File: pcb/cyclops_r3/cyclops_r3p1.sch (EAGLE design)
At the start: 48 parts, among them Q1 SUM11006, Q2 IRF510, U1 MCP4921, U2 317-N, U3 ADR03, U4 OP1177, U5 LM324N, U6 ZXTD45

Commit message: Minor changes.
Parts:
- removed R14: 560, cyclops:R_0603
- added R12: 560, cyclops:R_0603
- R10: value 1.1k -> 560
- R11: value 560 -> 1.1k
- renumbered C16 to C15
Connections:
- net +12V: now also R11.2; no longer R10.2
- net GND: now also R12.1; no longer R11.1
- net N$10: now also R10.1; no longer R14.1
- net N$13: now also R10.2, R11.1, R12.2; no longer R10.1, R11.2, R14.2
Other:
- note added: "GND LINK"
- moved on the sheet: R10, R11
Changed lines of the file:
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@@
 <part name="R5" library="cyclops" deviceset="R" device="_0603" value="470"/>
 <part name="R6" library="cyclops" deviceset="R" device="_0603" value="1k"/>
-<part name="C16" library="cyclops" deviceset="C" device="_0805" value="1uF"/>
+<part name="C15" library="cyclops" deviceset="C" device="_0805" value="1uF"/>
 <part name="C14" library="cyclops" deviceset="C" device="_0603" value=".1uF"/>
 <part name="SUPPLY30" library="cyclops" deviceset="AGND" device=""/>
@@
 <part name="SUPPLY31" library="cyclops" deviceset="AGND" device=""/>
 <part name="SUPPLY12" library="cyclops" deviceset="AGND" device=""/>
-<part name="SUPPLY17" library="cyclops" deviceset="AGND" device=""/>
 <part name="SUPPLY34" library="cyclops" deviceset="GND" device=""/>
 <part name="S3" library="cyclops" deviceset="SPDT" device="_CFPA" value="TEST"/>
@@
 <part name="SUPPLY35" library="cyclops" deviceset="AGND" device=""/>
 <part name="Q2" library="cyclops" deviceset="N-MOSFET" device="TO-262" value="IRF510"/>
-<part name="R14" library="cyclops" deviceset="R" device="_0603" value="560"/>
-<part name="R10" library="cyclops" deviceset="R" device="_0603" value="1.1k"/>
-<part name="R11" library="cyclops" deviceset="R" device="_0603" value="560"/>
+<part name="R10" library="cyclops" deviceset="R" device="_0603" value="560"/>
+<part name="R11" library="cyclops" deviceset="R" device="_0603" value="1.1k"/>
+<part name="R12" library="cyclops" deviceset="R" device="_0603" value="560"/>
 <part name="SUPPLY1" library="cyclops" deviceset="AGND" device=""/>
+<part name="SUPPLY4" library="cyclops" deviceset="GND" device=""/>
+<part name="SUPPLY29" library="cyclops" deviceset="GND" device=""/>
 </parts>
 <sheets>
@@
 <description>I/O Interface</description>
 <plain>
+<text x="147.32" y="27.94" size="1.778" layer="97">GND LINK</text>
 </plain>
 <instances>
@@
 <instance part="S1" gate="G$1" x="96.52" y="-33.02" rot="MR0"/>
 <instance part="SUPPLY12" gate="G$1" x="165.1" y="22.86"/>
-<instance part="SUPPLY17" gate="G$1" x="213.36" y="-10.16"/>
-<instance part="SUPPLY34" gate="PE" x="198.12" y="-10.16"/>
+<instance part="SUPPLY34" gate="PE" x="139.7" y="22.86"/>
 <instance part="S3" gate="G$1" x="127" y="-30.48" rot="R180"/>
+<instance part="SUPPLY4" gate="PE" x="60.96" y="10.16"/>
+<instance part="SUPPLY29" gate="PE" x="38.1" y="83.82"/>
 </instances>
 <busses>
@@
 <pinref part="U$1" gate="G$1" pin="5V"/>
 <wire x1="58.42" y1="17.78" x2="58.42" y2="12.7" width="0.1524" layer="91"/>
+<wire x1="58.42" y1="12.7" x2="53.34" y2="12.7" width="0.1524" layer="91"/>
+<label x="53.34" y="12.7" size="1.778" layer="95"/>
 </segment>
 </net>
@@
 <pinref part="U$1" gate="G$1" pin="D4"/>
 <wire x1="71.12" y1="78.74" x2="71.12" y2="91.44" width="0.1524" layer="91"/>
-<label x="71.12" y="83.82" size="1.778" layer="95" rot="R90"/>
+<label x="78.74" y="91.44" size="1.778" layer="95"/>
+<wire x1="71.12" y1="91.44" x2="86.36" y2="91.44" width="0.1524" layer="91"/>
 </segment>
 </net>
@@
 <segment>
 <pinref part="SUPPLY34" gate="PE" pin="GND"/>
-<wire x1="198.12" y1="-7.62" x2="198.12" y2="-2.54" width="0.1524" layer="91"/>
-<pinref part="SUPPLY17" gate="G$1" pin="AGND"/>
-<wire x1="198.12" y1="-2.54" x2="213.36" y2="-2.54" width="0.1524" layer="91"/>
-<wire x1="213.36" y1="-2.54" x2="213.36" y2="-7.62" width="0.1524" layer="91"/>
+<wire x1="139.7" y1="25.4" x2="139.7" y2="30.48" width="0.1524" layer="91"/>
+<wire x1="139.7" y1="30.48" x2="165.1" y2="30.48" width="0.1524" layer="91"/>
+<pinref part="U1" gate="G$1" pin="AVSS"/>
+<wire x1="165.1" y1="25.4" x2="165.1" y2="30.48" width="0.1524" layer="91"/>
+<pinref part="SUPPLY12" gate="G$1" pin="AGND"/>
+<wire x1="165.1" y1="30.48" x2="165.1" y2="33.02" width="0.1524" layer="91"/>
+<junction x="165.1" y="30.48"/>
 </segment>
 <segment>
@@
 </segment>
 <segment>
-<pinref part="U1" gate="G$1" pin="AVSS"/>
-<wire x1="165.1" y1="25.4" x2="165.1" y2="33.02" width="0.1524" layer="91"/>
-<pinref part="SUPPLY12" gate="G$1" pin="AGND"/>
-</segment>
-<segment>
 <pinref part="U$1" gate="G$1" pin="GND$2"/>
 <wire x1="60.96" y1="17.78" x2="60.96" y2="12.7" width="0.1524" layer="91"/>
-</segment>
-<segment>
+<pinref part="SUPPLY4" gate="PE" pin="GND"/>
 <pinref part="U$1" gate="G$1" pin="GND$1"/>
 <wire x1="63.5" y1="17.78" x2="63.5" y2="12.7" width="0.1524" layer="91"/>
-</segment>
-<segment>
+<wire x1="63.5" y1="12.7" x2="60.96" y2="12.7" width="0.1524" layer="91"/>
+<junction x="60.96" y="12.7"/>
+</segment>
+<segment>
+<pinref part="SUPPLY29" gate="PE" pin="GND"/>
+<wire x1="38.1" y1="86.36" x2="38.1" y2="88.9" width="0.1524" layer="91"/>
+<wire x1="38.1" y1="88.9" x2="43.18" y2="88.9" width="0.1524" layer="91"/>
 <pinref part="U$1" gate="G$1" pin="GND"/>
-<wire x1="43.18" y1="78.74" x2="43.18" y2="86.36" width="0.1524" layer="91"/>
+<wire x1="43.18" y1="78.74" x2="43.18" y2="88.9" width="0.1524" layer="91"/>
 </segment>
 </net>
@@
 <instance part="SUPPLY21" gate="G$1" x="40.64" y="93.98"/>
 <instance part="SUPPLY25" gate="G$1" x="53.34" y="93.98"/>
-<instance part="C16" gate="C" x="53.34" y="109.22"/>
+<instance part="C15" gate="C" x="53.34" y="109.22"/>
 <instance part="C14" gate="C" x="40.64" y="109.22"/>
 <instance part="SUPPLY30" gate="G$1" x="-10.16" y="60.96"/>
@@
 <instance part="SUPPLY35" gate="G$1" x="71.12" y="63.5"/>
 <instance part="Q2" gate="G$1" x="165.1" y="86.36"/>
-<instance part="R14" gate="R" x="124.46" y="83.82"/>
-<instance part="R10" gate="R" x="134.62" y="96.52" rot="R90"/>
-<instance part="R11" gate="R" x="134.62" y="71.12" rot="R90"/>
+<instance part="R10" gate="R" x="124.46" y="83.82"/>
+<instance part="R11" gate="R" x="134.62" y="96.52" rot="R90"/>
+<instance part="R12" gate="R" x="134.62" y="71.12" rot="R90"/>
 <instance part="SUPPLY1" gate="G$1" x="134.62" y="45.72"/>
 </instances>
@@
 <segment>
 <pinref part="SUPPLY25" gate="G$1" pin="AGND"/>
-<pinref part="C16" gate="C" pin="2"/>
+<pinref part="C15" gate="C" pin="2"/>
 <wire x1="53.34" y1="96.52" x2="53.34" y2="104.14" width="0.1524" layer="91"/>
 </segment>
@@
 <segment>
 <pinref part="SUPPLY1" gate="G$1" pin="AGND"/>
-<pinref part="R11" gate="R" pin="1"/>
+<pinref part="R12" gate="R" pin="1"/>
 <wire x1="134.62" y1="48.26" x2="134.62" y2="66.04" width="0.1524" layer="91"/>
 </segment>
@@
 <pinref part="C14" gate="C" pin="1"/>
 <wire x1="40.64" y1="121.92" x2="40.64" y2="111.76" width="0.1524" layer="91"/>
-<pinref part="C16" gate="C" pin="1"/>
+<pinref part="C15" gate="C" pin="1"/>
 <wire x1="40.64" y1="121.92" x2="53.34" y2="121.92" width="0.1524" layer="91"/>
 <wire x1="53.34" y1="121.92" x2="53.34" y2="111.76" width="0.1524" layer="91"/>
@@
 <junction x="66.04" y="121.92"/>
 <label x="147.32" y="121.92" size="1.778" layer="95"/>
-<pinref part="R10" gate="R" pin="2"/>
+<pinref part="R11" gate="R" pin="2"/>
 <wire x1="134.62" y1="121.92" x2="167.64" y2="121.92" width="0.1524" layer="91"/>
 <wire x1="134.62" y1="101.6" x2="134.62" y2="121.92" width="0.1524" layer="91"/>
@@
 <wire x1="114.3" y1="83.82" x2="114.3" y2="76.2" width="0.1524" layer="91"/>
 <wire x1="114.3" y1="76.2" x2="109.22" y2="76.2" width="0.1524" layer="91"/>
-<pinref part="R14" gate="R" pin="1"/>
+<pinref part="R10" gate="R" pin="1"/>
 <wire x1="119.38" y1="83.82" x2="114.3" y2="83.82" width="0.1524" layer="91"/>
 <junction x="114.3" y="83.82"/>
@@
 <segment>
 <pinref part="Q2" gate="G$1" pin="G"/>
-<pinref part="R14" gate="R" pin="2"/>
+<pinref part="R10" gate="R" pin="2"/>
 <wire x1="162.56" y1="83.82" x2="134.62" y2="83.82" width="0.1524" layer="91"/>
-<pinref part="R10" gate="R" pin="1"/>
+<pinref part="R11" gate="R" pin="1"/>
 <wire x1="134.62" y1="83.82" x2="129.54" y2="83.82" width="0.1524" layer="91"/>
 <wire x1="134.62" y1="83.82" x2="134.62" y2="91.44" width="0.1524" layer="91"/>
 <junction x="134.62" y="83.82"/>
-<pinref part="R11" gate="R" pin="2"/>
+<pinref part="R12" gate="R" pin="2"/>
 <wire x1="134.62" y1="83.82" x2="134.62" y2="76.2" width="0.1524" layer="91"/>
 </segment>
@@
 </sheet>
 </sheets>
+<errors>
+</errors>
 </schematic>
 </drawing>

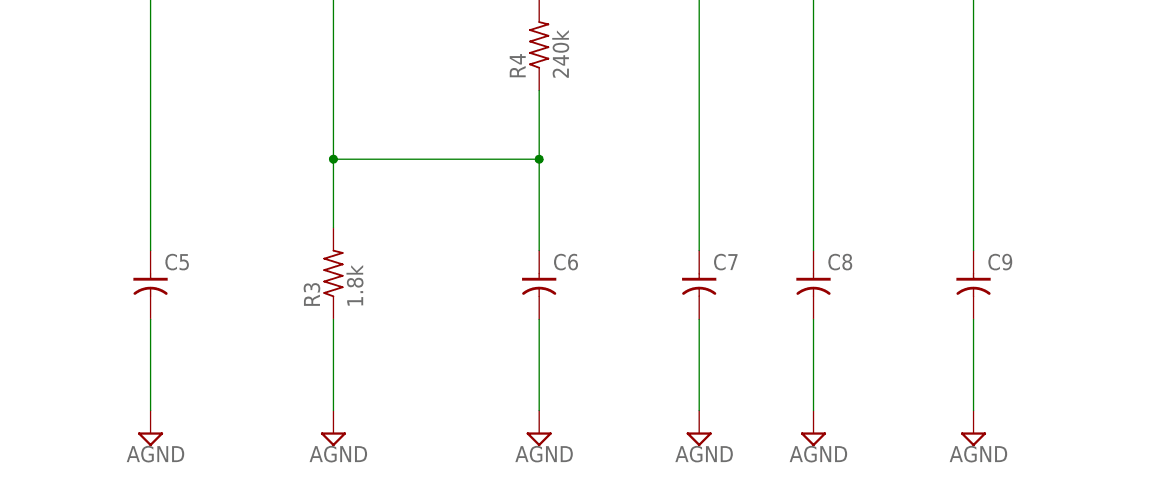
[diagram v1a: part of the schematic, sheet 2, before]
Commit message: Small routing improvement.
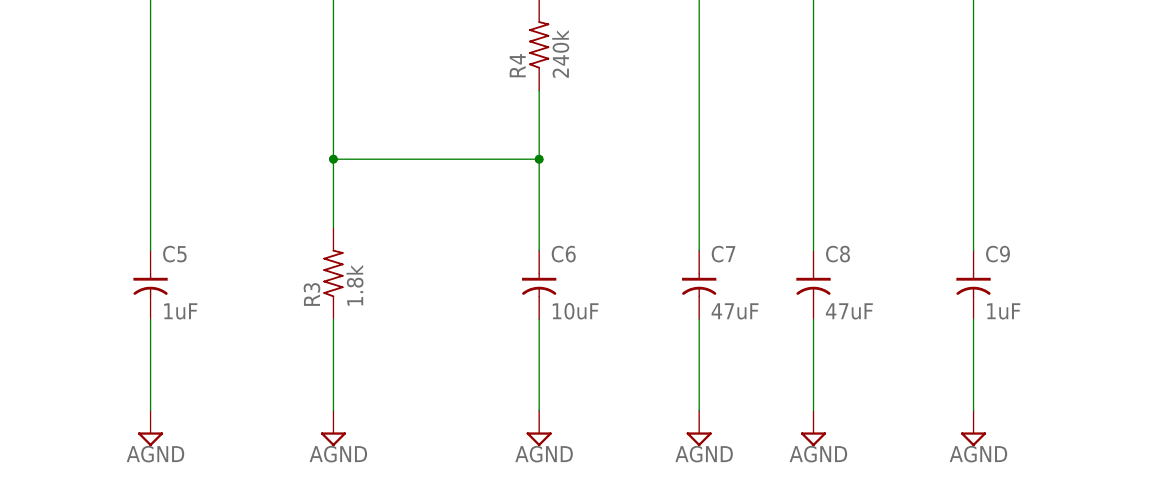
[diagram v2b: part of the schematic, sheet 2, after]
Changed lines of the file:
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@@
 <instance part="SUPPLY9" gate="G$1" x="86.36" y="-58.42"/>
 <instance part="SUPPLY10" gate="G$1" x="104.14" y="-58.42"/>
-<instance part="C5" gate="C" x="12.7" y="-43.18" smashed="yes">
-<attribute name="NAME" x="14.224" y="-40.259" size="1.778" layer="95"/>
-</instance>
-<instance part="C6" gate="C" x="55.88" y="-43.18" smashed="yes">
-<attribute name="NAME" x="57.404" y="-40.259" size="1.778" layer="95"/>
-</instance>
-<instance part="C9" gate="C" x="104.14" y="-43.18" smashed="yes">
-<attribute name="NAME" x="105.664" y="-40.259" size="1.778" layer="95"/>
-</instance>
-<instance part="C8" gate="C" x="86.36" y="-43.18" smashed="yes">
-<attribute name="NAME" x="87.884" y="-40.259" size="1.778" layer="95"/>
-</instance>
+<instance part="C5" gate="C" x="12.7" y="-43.18"/>
+<instance part="C6" gate="C" x="55.88" y="-43.18"/>
+<instance part="C9" gate="C" x="104.14" y="-43.18"/>
+<instance part="C8" gate="C" x="86.36" y="-43.18"/>
 <instance part="SUPPLY11" gate="G$1" x="12.7" y="-58.42"/>
 <instance part="Q1" gate="G$1" x="-27.94" y="-7.62" smashed="yes" rot="R90">
@@
 <instance part="FRAME2" gate="G$1" x="-109.22" y="-147.32"/>
 <instance part="FRAME2" gate="G$2" x="63.5" y="-147.32"/>
-<instance part="C7" gate="C" x="73.66" y="-43.18" smashed="yes">
-<attribute name="NAME" x="75.184" y="-40.259" size="1.778" layer="95"/>
-</instance>
+<instance part="C7" gate="C" x="73.66" y="-43.18"/>
 <instance part="SUPPLY31" gate="G$1" x="73.66" y="-58.42"/>
 </instances>

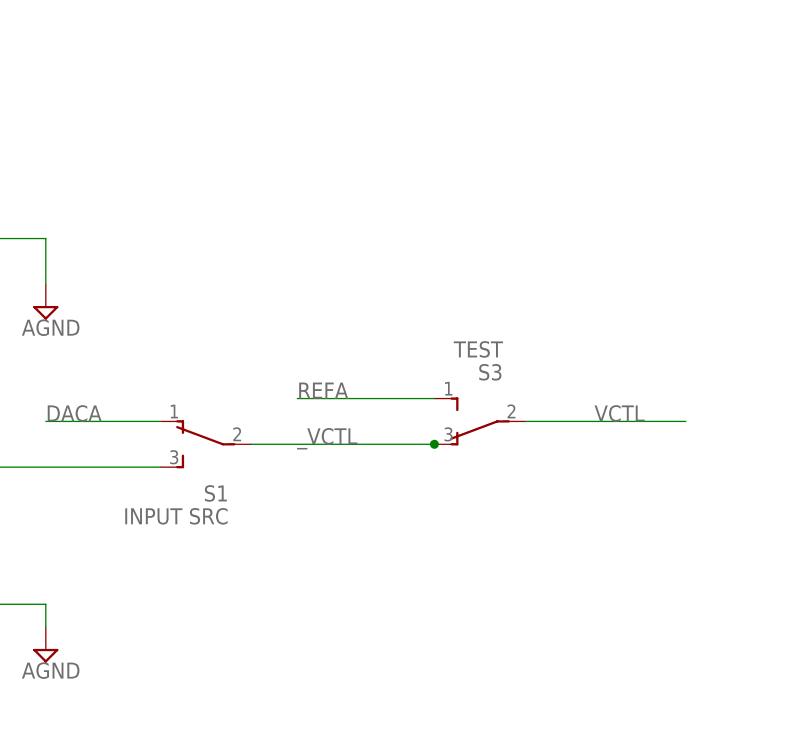
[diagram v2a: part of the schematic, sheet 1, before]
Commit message: Added a low profile BNC connection for getting input from an amplified photodiode.
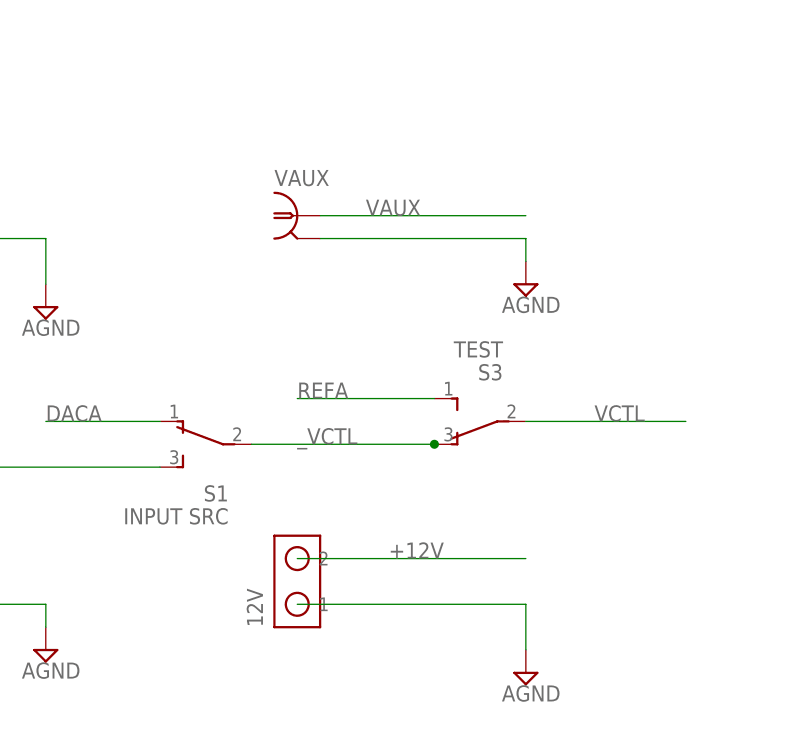
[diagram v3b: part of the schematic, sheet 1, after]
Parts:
- added 12V: SCREW2, cyclops:SCREW2
- added VAUX: (no value), cyclops:BNC_V-BITE
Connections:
- net +12V: now also 12V.2
- net GND: now also 12V.1, VAUX.2
- net VAUX: now also VAUX.1
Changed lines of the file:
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@@
 <part name="SUPPLY4" library="cyclops" deviceset="GND" device=""/>
 <part name="SUPPLY29" library="cyclops" deviceset="GND" device=""/>
+<part name="VAUX" library="cyclops" deviceset="BNC" device="_V-BITE"/>
+<part name="SUPPLY17" library="cyclops" deviceset="AGND" device=""/>
+<part name="12V" library="cyclops" deviceset="SCREW2" device=""/>
+<part name="SUPPLY36" library="cyclops" deviceset="AGND" device=""/>
 </parts>
 <sheets>
@@
 <instance part="SUPPLY4" gate="PE" x="60.96" y="10.16"/>
 <instance part="SUPPLY29" gate="PE" x="38.1" y="83.82"/>
+<instance part="VAUX" gate="G$1" x="104.14" y="-7.62"/>
+<instance part="SUPPLY17" gate="G$1" x="129.54" y="-15.24"/>
+<instance part="12V" gate="G$1" x="104.14" y="-50.8" rot="R90"/>
+<instance part="SUPPLY36" gate="G$1" x="129.54" y="-58.42"/>
 </instances>
 <busses>
@@
 <label x="50.8" y="-15.24" size="1.778" layer="95"/>
 </segment>
+<segment>
+<pinref part="12V" gate="G$1" pin="2"/>
+<wire x1="104.14" y1="-45.72" x2="129.54" y2="-45.72" width="0.1524" layer="91"/>
+<label x="114.3" y="-45.72" size="1.778" layer="95"/>
+</segment>
 </net>
 <net name="LED-" class="0">
@@
 <wire x1="43.18" y1="78.74" x2="43.18" y2="88.9" width="0.1524" layer="91"/>
 </segment>
+<segment>
+<pinref part="VAUX" gate="G$1" pin="2"/>
+<wire x1="106.68" y1="-10.16" x2="129.54" y2="-10.16" width="0.1524" layer="91"/>
+<wire x1="129.54" y1="-10.16" x2="129.54" y2="-12.7" width="0.1524" layer="91"/>
+<pinref part="SUPPLY17" gate="G$1" pin="AGND"/>
+</segment>
+<segment>
+<pinref part="12V" gate="G$1" pin="1"/>
+<wire x1="104.14" y1="-50.8" x2="129.54" y2="-50.8" width="0.1524" layer="91"/>
+<pinref part="SUPPLY36" gate="G$1" pin="AGND"/>
+<wire x1="129.54" y1="-50.8" x2="129.54" y2="-55.88" width="0.1524" layer="91"/>
+</segment>
 </net>
 <net name="VAUX" class="0">
@@
 <label x="50.8" y="-45.72" size="1.778" layer="95"/>
 </segment>
-</net>
+<segment>
+<pinref part="VAUX" gate="G$1" pin="1"/>
+<wire x1="106.68" y1="-7.62" x2="129.54" y2="-7.62" width="0.1524" layer="91"/>
+<label x="111.76" y="-7.62" size="1.778" layer="95"/>
+</segment>
+</net>

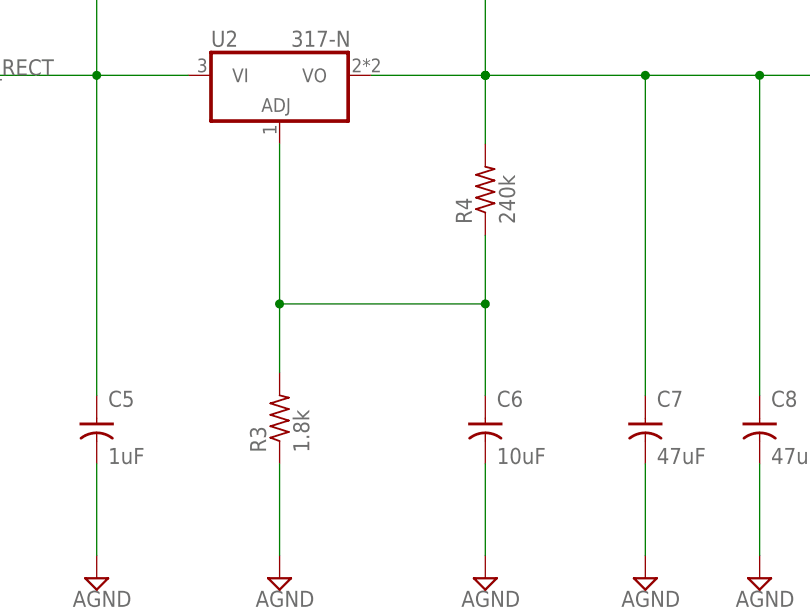
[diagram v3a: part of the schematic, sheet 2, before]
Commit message: Added a note concerning the location of the MOSFET pre-biasing.
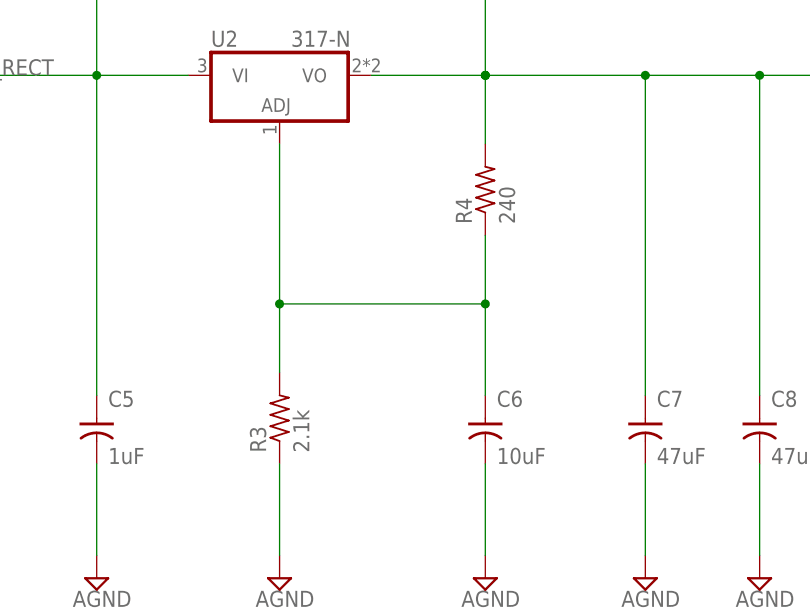
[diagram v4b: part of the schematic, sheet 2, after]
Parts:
- R3: value 1.8k -> 2.1k
- R4: value 240k -> 240
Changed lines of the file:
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@@
 <part name="U2" library="cyclops" deviceset="*317" device="_TO263" value="317-N"/>
 <part name="D2" library="cyclops" deviceset="DIODE" device="S1B-13-F" value="S1B"/>
-<part name="R3" library="cyclops" deviceset="R" device="_0603" value="1.8k"/>
-<part name="R4" library="cyclops" deviceset="R" device="_0603" value="240k"/>
+<part name="R3" library="cyclops" deviceset="R" device="_0603" value="2.1k"/>
+<part name="R4" library="cyclops" deviceset="R" device="_0603" value="240"/>
 <part name="SUPPLY3" library="cyclops" deviceset="AGND" device=""/>
 <part name="SUPPLY8" library="cyclops" deviceset="AGND" device=""/>
